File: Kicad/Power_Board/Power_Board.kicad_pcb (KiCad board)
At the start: 2 copper layers, 27.9 x 14 mm, 17 parts, among them J1 Conn_01x04_Pin, U1 PTPS543021DRLR, U2 PTPS543021DRLR

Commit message: Main Board v1
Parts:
- C4: value 33u -> 44u
- L1: value 10uH -> 6.8uH
- R5: value 13.3k -> 22.1k
- moved C1 1.07 mm to (59.4, 68.9)
- moved C2 1.07 mm to (61.5, 68.8)
- moved C5 1.02 mm to (75.9, 70.9)
- moved C8 1.02 mm to (75.7, 77.0)
- moved L1 1.02 mm to (71.3, 67.1)
- moved L2 1.02 mm to (71.4, 73.2)
- moved R5 1.02 mm to (79.0, 69.5)
- moved R7 1.02 mm to (76.7, 74.0)
- moved U1 1.02 mm to (64.5, 67.6)
- moved U2 1.02 mm to (64.5, 73.7)
- moved C3 1.02 mm to (67.8, 67.1)
- moved C4 1.02 mm to (74.7, 67.8)
- moved C6 1.02 mm to (67.8, 73.2)
- moved C7 1.02 mm to (74.2, 73.9)
- moved J1 1.02 mm to (82.8, 74.7)
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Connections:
- net Net-(J1-Pin_1) renamed /12v Output
- net Net-(J1-Pin_4) renamed /3v3 Output
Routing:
- net /Cleaned VIN: track 15.9 -> 0.00 mm
- net GND: track 13.6 -> 10.8 mm
- added copper zone on F.Cu, net /Cleaned VIN

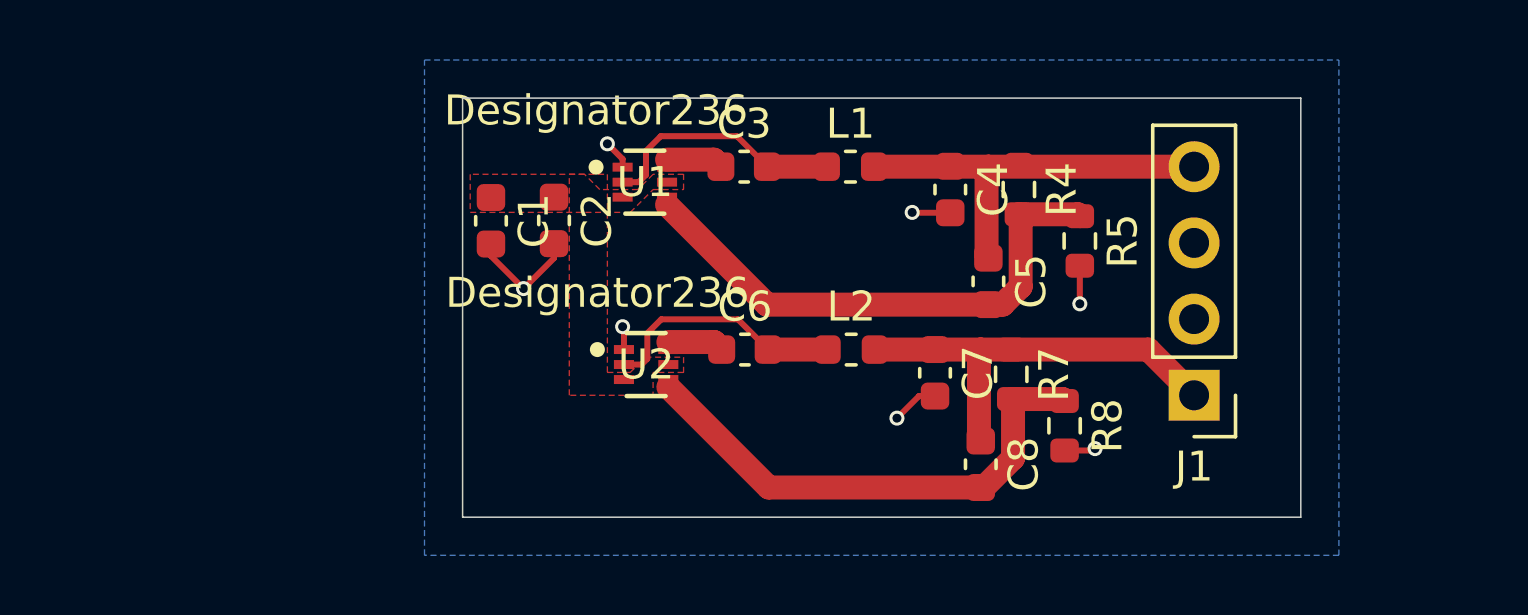
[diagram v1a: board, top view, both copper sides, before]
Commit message: Created cad for how the boards will fit together
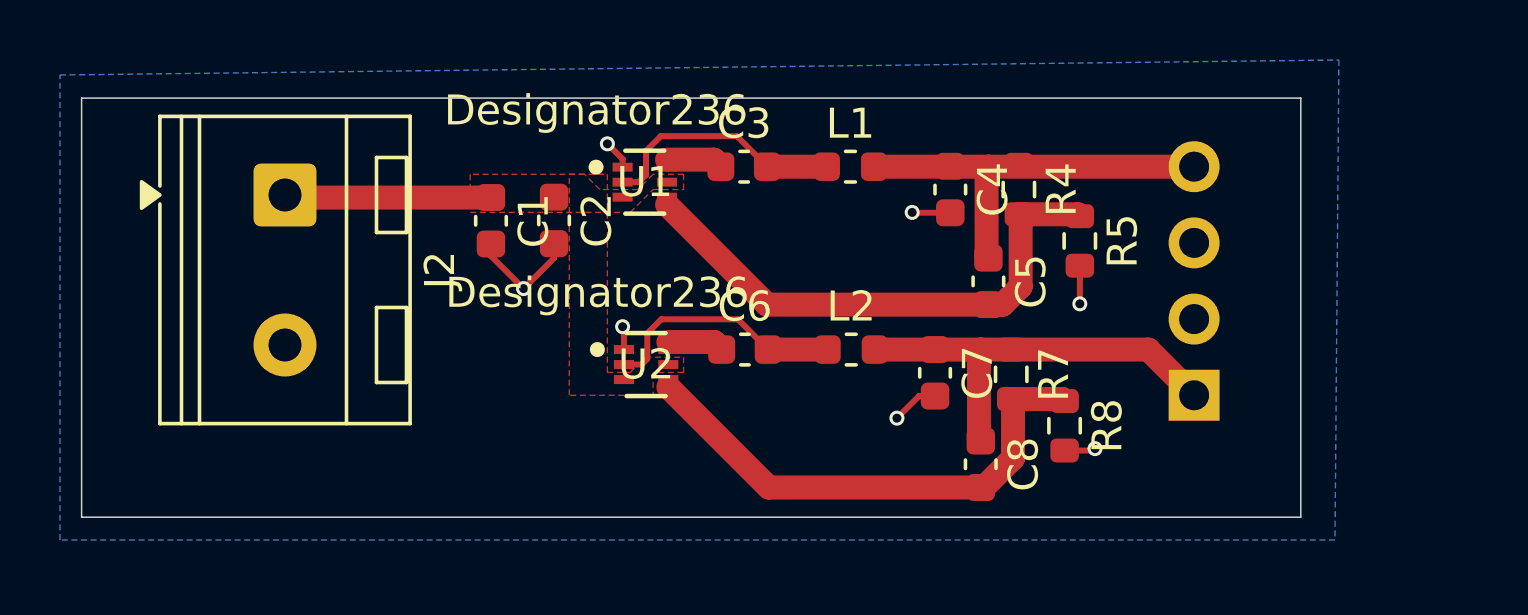
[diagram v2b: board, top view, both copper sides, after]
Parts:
- added J2: Screw_Terminal_01x02, TerminalBlock_RND:TerminalBlock_RND_205-00045_1x02_P5.00mm_Horizontal, F.Cu at (52.5, 68.0)
- J1: footprint Connector_PinHeader_2.54mm:PinHeader_1x04_P2.54mm_Vertical -> Connector_PinSocket_2.54mm:PinSocket_1x04_P2.54mm_Vertical; moved to B.Cu
- turned J1 to 0 degrees
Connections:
- net /Cleaned VIN renamed /20V VIN
- net Net-(U1-BOOT) renamed /Boot
- net Net-(U1-SW) renamed /SW
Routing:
- net /20V VIN: track 0.00 -> 6.90 mm
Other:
- board size 27.9 x 14 mm -> 40.6 x 14 mm

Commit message: Wrote v1 of the code, final version of boards
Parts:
- added G***: LOGO, LOGO, F.Cu at (60.3, 74.8)
- C1: value 10u -> 10uF; footprint Capacitor_SMD:C_0603_1608Metric -> PCM_JLCPCB:C_0603
- C2, C3, C6: value 0.1u -> 100nF; footprint Capacitor_SMD:C_0603_1608Metric -> PCM_JLCPCB:C_0603
- C4: value 44u -> 47uF; footprint Capacitor_SMD:C_0603_1608Metric -> PCM_JLCPCB:C_0805
- C5: value 75p -> 68pF; footprint Capacitor_SMD:C_0603_1608Metric -> PCM_JLCPCB:C_0603
- C7: value 60u -> 22uF; footprint Capacitor_SMD:C_0603_1608Metric -> PCM_JLCPCB:C_0805
- C8: value 100p -> 100pF; footprint Capacitor_SMD:C_0603_1608Metric -> PCM_JLCPCB:C_0603
- L1: footprint Inductor_SMD:L_0603_1608Metric -> Inductor_SMD:L_TDK_VLS6045EX_VLS6045AF
- L2: value 5uH -> 4.7uH; footprint Inductor_SMD:L_0603_1608Metric -> Inductor_SMD:L_TDK_VLS6045EX_VLS6045AF
- R4, R7: value 100k -> 100kΩ; footprint Resistor_SMD:R_0603_1608Metric -> PCM_JLCPCB:R_0603
- R5: value 22.1k -> 22kΩ; footprint Resistor_SMD:R_0603_1608Metric -> PCM_JLCPCB:R_0603
- R8: value 5.25k -> 5.1kΩ; footprint Resistor_SMD:R_0603_1608Metric -> PCM_JLCPCB:R_0603
- moved C5 3.62 mm to (79.6, 70.8)
- moved C8 3.62 mm to (79.3, 76.9)
- moved J1 3.62 mm to (86.4, 74.6)
- moved R5 3.62 mm to (82.6, 69.4)
- moved R7 3.62 mm to (80.3, 73.9)
- moved R4 3.62 mm to (80.6, 67.7)
- moved R8 3.62 mm to (82.1, 75.6)
- moved C7 3.28 mm to (77.5, 73.8)
- moved C4 2.88 mm to (77.5, 67.7)
- moved L2 2.30 mm to (72.8, 75.0)
- moved L1 1.84 mm to (72.8, 68.2)
- moved U1 0.22 mm to (64.3, 67.6), turned to -90 degrees
- turned U2 to -90 degrees
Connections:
- net Net-(U1-FB) renamed /FB
- net Net-(U2-BOOT) renamed /BOOT 12V
- net Net-(U2-FB) renamed /FB 12V
- net Net-(U2-SW) renamed /SW 12V
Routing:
- net /SW: track 8.33 -> 2.56 mm
- net /SW 12V: track 8.33 -> 2.80 mm
- net /FB 12V: track 17.1 -> 22.5 mm
- net /FB: track 17.9 -> 23.2 mm
- net /20V VIN: track 6.90 -> 9.01 mm
- net /Boot: track 1.89 -> 0.00 mm
- net /BOOT 12V: track 1.88 -> 0.00 mm
- net /12v Output: track 14.4 -> 16.2 mm
- net /3v3 Output: track 13.8 -> 15.4 mm
- added copper zone on F.Cu, net /BOOT 12V
- added copper zone on F.Cu, net /Boot
- added copper zone on F.Cu, net /SW
- added copper zone on F.Cu, net /SW 12V
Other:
- board size 40.6 x 14 mm -> 40.8 x 13.8 mm

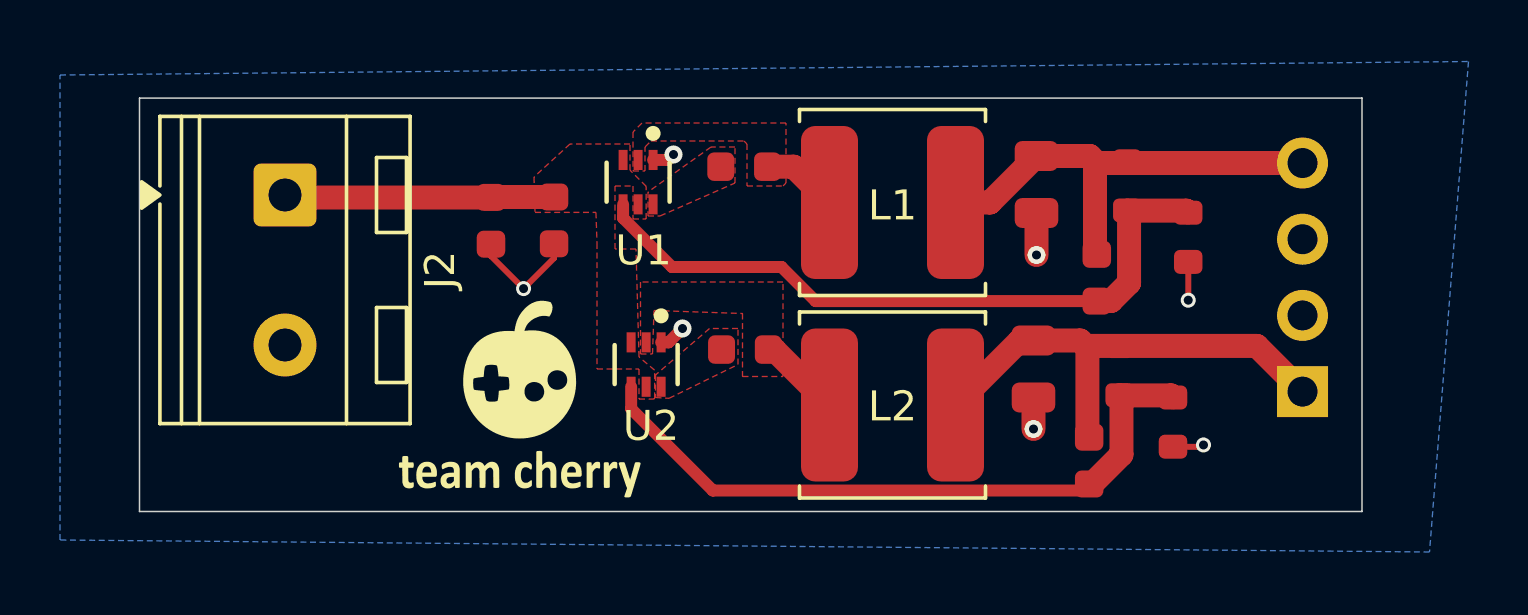
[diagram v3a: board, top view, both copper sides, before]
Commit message: Updated to use 0805 instead of JLC assembly
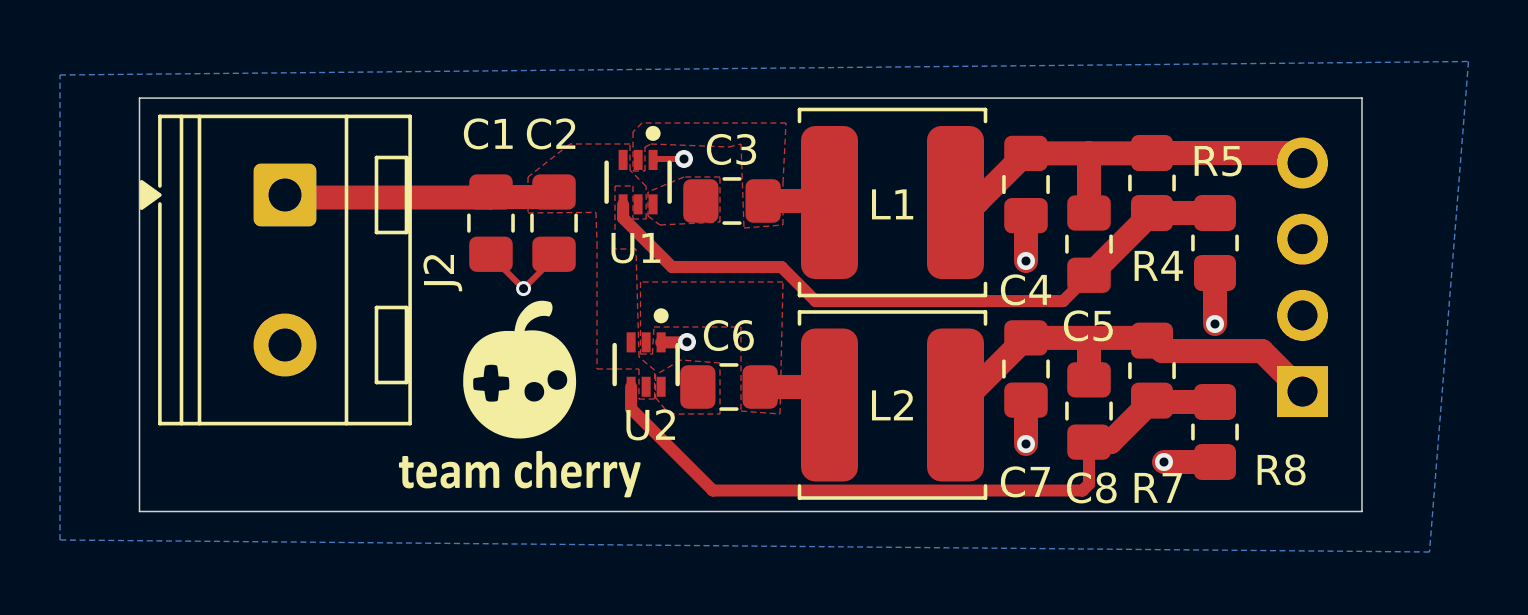
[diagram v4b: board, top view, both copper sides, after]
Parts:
- C1, C2, C3, C5, C6, C8: footprint PCM_JLCPCB:C_0603 -> Capacitor_SMD:C_0805_2012Metric_Pad1.18x1.45mm_HandSolder
- C4, C7: footprint PCM_JLCPCB:C_0805 -> Capacitor_SMD:C_0805_2012Metric_Pad1.18x1.45mm_HandSolder
- R4, R5, R7, R8: footprint PCM_JLCPCB:R_0603 -> Resistor_SMD:R_0805_2012Metric_Pad1.20x1.40mm_HandSolder
- moved C8 1.65 mm to (79.3, 75.2)
- moved R8 1.44 mm to (83.5, 75.9)
- moved C6 1.36 mm to (67.3, 74.4)
- moved C3 1.21 mm to (67.4, 68.2)
- moved C5 1.15 mm to (79.3, 69.6)
- moved R7 1.08 mm to (81.4, 73.9)
- moved R5 0.91 mm to (83.5, 69.6)
- moved R4 0.83 mm to (81.4, 67.6)
- moved C4 0.35 mm to (77.2, 67.7)
- moved C7 0.25 mm to (77.2, 73.8)
- moved C2 0.09 mm to (61.5, 68.9)
- moved C1 0.08 mm to (59.4, 68.9)
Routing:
- net GND: track 10.3 -> 12.2 mm
- net /12v Output: track 16.2 -> 14.6 mm
- net /3v3 Output: track 15.4 -> 14.4 mm
- net /FB 12V: track 22.5 -> 23.5 mm
- net /FB: track 23.2 -> 22.6 mm
